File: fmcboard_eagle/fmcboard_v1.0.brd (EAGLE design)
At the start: 98 x 74 mm, 7 parts, among them J1 8pin, J12 4p-2.54, J2 ASP-134604-01

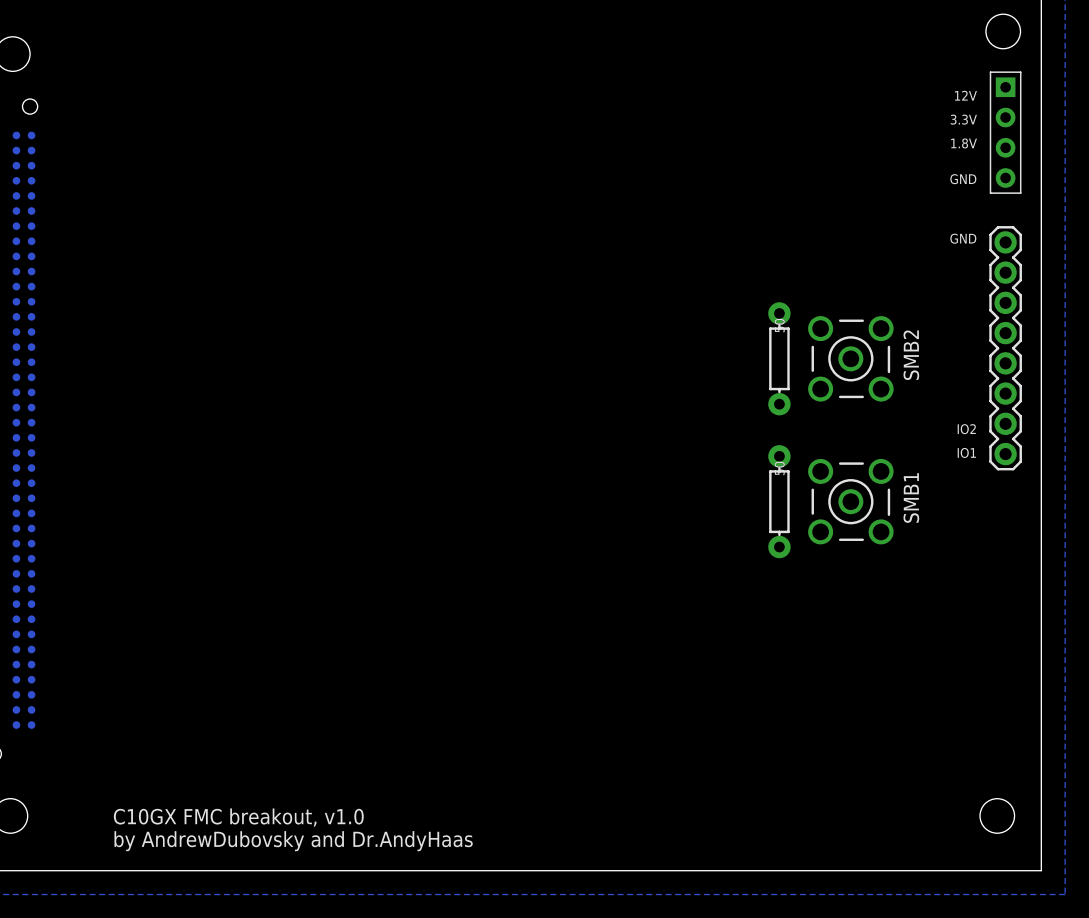
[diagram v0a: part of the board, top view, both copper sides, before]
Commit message: added two op amps to condition input and added GPIO breakout
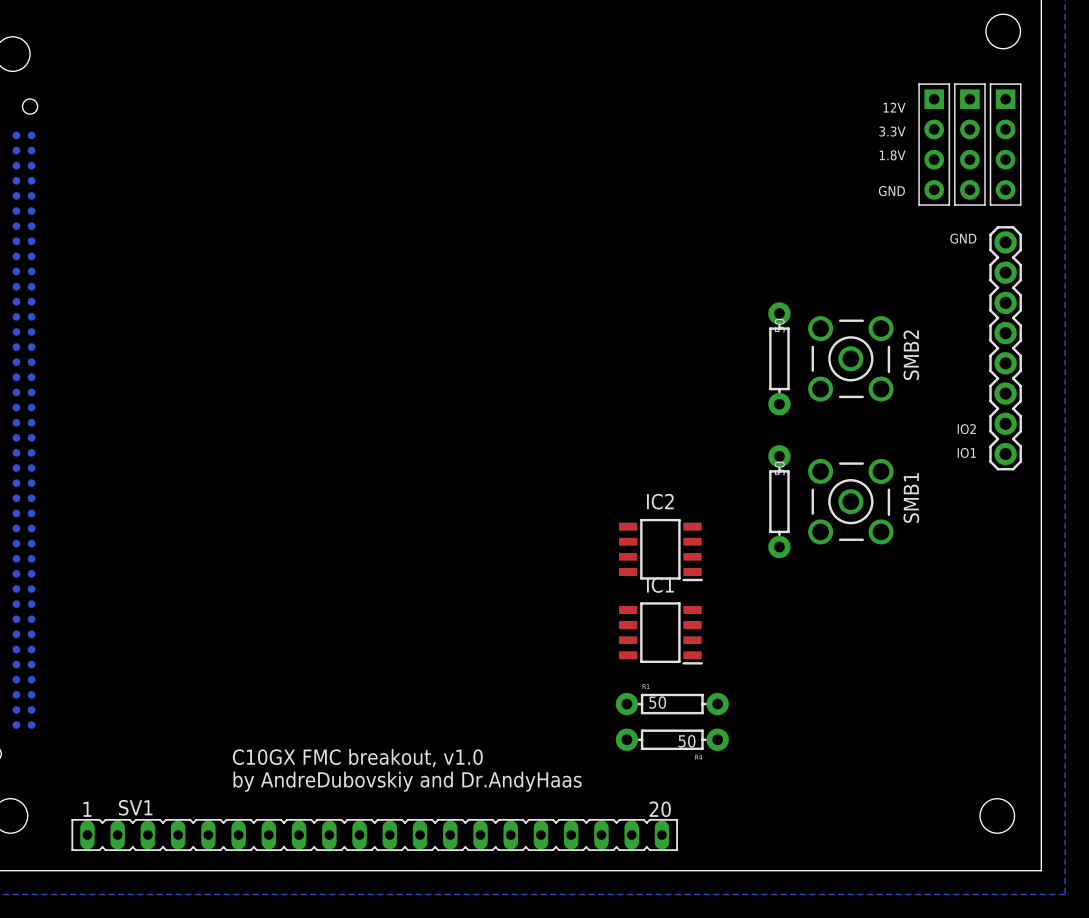
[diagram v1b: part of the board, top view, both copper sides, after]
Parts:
- added IC1, IC2: OPA699ID, OPA699ID:SOIC127P600X175-8N
- added J3, J4: 4p-2.54, Seeed-Connector:H4-2.54
- added R1, R4: 50, SparkFun-Resistors:AXIAL-0.3
- added SV1: (no value), con-lsta:FE20
- moved J12 6.08 mm to (89.0, 61.0)
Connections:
- removed net N$2: J1.3
- removed net N$4: J1.5
- removed net N$5: J1.4
- removed net N$6: J1.6
- new net +VS: IC1.7, IC2.7, J1.3
- new net -VS: IC1.4, IC2.4, J1.4
- new net N$1: IC1.3, IC2.2, IC2.6
- new net N$10: J2.H8, SV1.5
- new net N$11: J2.H4, SV1.3
- new net N$12: J2.H10, SV1.6
- new net N$13: J2.H11, SV1.7
- new net N$14: J2.H13, SV1.8
- new net N$15: J2.H14, SV1.9
- new net N$16: J2.H16, SV1.10
- new net N$17: J2.H17, SV1.11
- new net N$18: J2.H19, SV1.12
- new net N$19: J2.H20, SV1.13
- new net N$20: J2.H22, SV1.14
- new net N$21: J2.H23, SV1.15
- new net N$22: J2.H25, SV1.16
- new net N$23: J2.H26, SV1.17
- new net N$24: J2.H28, SV1.18
- new net N$25: J2.H29, SV1.19
- new net N$26: J2.H31, SV1.20
- new net N$3: IC1.2, R1.P$2, R4.P$1
- new net N$8: J2.H1, SV1.1
- new net N$9: J2.H2, SV1.2
- new net VH: IC1.8, IC2.8, J1.5
- new net VL: IC1.5, IC2.5, J1.6
- net 12V: now also J3.1, J4.1
- net 1V8: now also J3.3, J4.3
- net 3V3: now also J3.2, J4.2
- net GND: now also J2.H12, J2.H15, J2.H18, J2.H21, J2.H24, J2.H27, J2.H3, J2.H30, J2.H33, J2.H36, J2.H39, J2.H6, J2.H9, J3.4, J4.4, R4.P$2
- net IO1: now also IC2.3
- net IO2: now also IC1.6, J2.H7, R1.P$1, SV1.4
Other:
- board text added: "C10GX FMC breakout, v1.0 by AndreDubovskiy and Dr.AndyHaas"
- board text removed: "C10GX FMC breakout, v1.0 by AndrewDubovsky and Dr.AndyHaas"

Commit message: board v1 work with Andre
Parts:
- added C1, C2, C4, C6: 10uF, SparkFun-Capacitors:CAP-PTH-5MM
- added C10, C11, C12, C13, C14, C3, C5, C7, C8, C9: 0.1uF, SparkFun-Passives:0805
- added IC3, IC4: ICL7660CPA, maxim:DIL08
- added J5: 8pin, SparkFun-Connectors:1X08
- added PCB1: ARDUINO_NANO, E14_Arduino_revC:ARDUINO_NANO
- added R5: 10k, SparkFun-Resistors:AXIAL-0.3
- added R6: 50, SparkFun-Resistors:AXIAL-0.3
- added R7, R8: 100k, resistor:RTRIM3296W
- added SMB3: BU-SMB-V, con-coax:BU-SMB-V
- added SV2: 20, con-lsta:FE20
- added U1: TXS0108EPWR-TSSOP20, Seeed-IC:TSSOP20-0.65-6.5X4.4MM
- R1: value 50 -> 750
- R3: value 50 -> 10k
- R4: value 50 -> 150
- SV1: value (none) -> 20
- moved R3 112.7 mm to (2.00, -42.0), turned to 0 degrees
- moved J12 37.7 mm to (57.0, 41.0)
- moved J3 37.7 mm to (63.0, 41.0)
- moved J4 37.7 mm to (60.0, 41.0)
- moved SV1 30.6 mm to (23.0, 27.0), turned to 90 degrees
- moved R2 7.28 mm to (78.0, 38.0)
- moved SMB1 7.28 mm to (84.0, 38.0)
- moved SMB2 6.32 mm to (84.0, 49.0)
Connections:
- net N$16 renamed H16
- net N$17 renamed H17
- removed net IO2: IC1.6, J1.2, J2.H7, R1.P$1, R3.P$2, SMB2.1, SV1.4
- removed net N$10: J2.H8, SV1.5
- removed net N$11: J2.H4, SV1.3
- removed net N$12: J2.H10, SV1.6
- removed net N$13: J2.H11, SV1.7
- removed net N$14: J2.H13, SV1.8
- removed net N$15: J2.H14, SV1.9
- removed net N$18: J2.H19, SV1.12
- removed net N$19: J2.H20, SV1.13
- removed net N$20: J2.H22, SV1.14
- removed net N$21: J2.H23, SV1.15
- removed net N$22: J2.H25, SV1.16
- removed net N$23: J2.H26, SV1.17
- removed net N$24: J2.H28, SV1.18
- removed net N$25: J2.H29, SV1.19
- removed net N$26: J2.H31, SV1.20
- removed net N$7: J1.7
- removed net N$8: J2.H1, SV1.1
- removed net N$9: J2.H2, SV1.2
- new net AR_SCLIN: J5.7, PCB1.D9, U1.8
- new net AR_SDAIN: J5.6, PCB1.D11, U1.3
- new net H13: J2.H13, SV1.7
- new net H14: J2.H14, SV1.8
- new net H19: J2.H19, SV1.13
- new net H20: J2.H20, SV1.14
- new net H22: J2.H22, SV1.16
- new net H23: J2.H23, SV1.17
- new net H25: J2.H25, SV1.19
- new net H26: J2.H26, SV1.20
- new net H27: J2.H28, SV2.1
- new net H28: J2.H29, SV2.2
- new net H31: J2.H31, SV2.4
- new net H32: J2.H32, SV2.5
- new net H34: J2.H34, SV2.7
- new net H35: J2.H35, SV2.8
- new net H37: J2.H37, SV2.10
- new net H38: J2.H38, SV2.11
- new net IO2_H11: J2.H11, J5.2, R6.P$2, SMB3.1, SV1.5
- new net N$2: C4.1, IC3.2
- new net N$4: C4.2, IC3.4
- new net N$5: C1.1, IC4.2
- new net N$6: C1.2, IC4.4
- new net OFFSETIN1: C11.1, J5.4, R5.P$2
- new net OPBUF1: IC2.2, IC2.6, J5.5, R3.P$2
- new net OPOUT1_H10: IC1.6, J2.H10, J5.3, R1.P$1, SMB2.1, SV1.4
- new net SCLIN: J2.H7, SV1.1, U1.13
- new net SDAIN: J2.H8, SV1.2, U1.18
- net +VS: now also C3.1, C9.1, IC3.8, IC4.8, PCB1.5V, R7.3, U1.19
- net -VS: now also C10.1, C2.1, C6.1, IC3.5, IC4.5, R8.3
- net 12V: now also C12.1, J2.C37
- net 1V8: now also C14.1, C5.1, J2.H40, U1.10, U1.2
- net 3V3: now also C13.1, J2.D40
- net GND: now also C10.2, C11.2, C12.2, C13.2, C14.2, C2.2, C3.2, C5.2, C6.2, C7.2, C8.2, C9.2, IC3.3, IC4.3, J1.1, J1.2, J1.7, J5.8, PCB1.GND, R6.P$1, R7.1, R8.1, SMB3.2, SMB3.3, SMB3.4, SMB3.5, SV2.17, SV2.18, SV2.19, SV2.20, U1.11; no longer R3.P$1
- net IO1: now also J5.1; no longer J1.1
- net N$1: now also R3.P$1, R5.P$1; no longer IC2.2, IC2.6
- net VH: now also C7.1, R7.2
- net VL: now also C8.1, R8.2
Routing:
- added copper zone on layer 2, net GND

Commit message: first draft of pcb routing
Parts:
- removed PCB1: ARDUINO_NANO, E14_Arduino_revC:ARDUINO_NANO
- added ARDUINO_NANO1: (no value), ArduinoNanoV30:ARDUINO_NANO
- moved C14 152.6 mm to (58.0, 68.0), flipped to the bottom, turned to 180 degrees
- moved R8 141.5 mm to (55.0, 26.0), turned to 90 degrees
- moved C5 141.2 mm to (66.0, 66.0), flipped to the bottom, turned to 180 degrees
- moved R7 126.2 mm to (54.0, 14.0)
- moved C12 126.1 mm to (50.0, 45.0), turned to 180 degrees
- moved C13 125.9 mm to (50.0, 42.0), turned to 180 degrees
- moved C11 125.5 mm to (77.0, 15.0)
- moved C10 123.4 mm to (72.0, 21.0), turned to 270 degrees
- moved R6 106.8 mm to (38.0, 10.0), turned to 180 degrees
- moved C9 106.7 mm to (58.0, 18.0), turned to 180 degrees
- moved C8 106.2 mm to (57.0, 22.0), turned to 180 degrees
- moved SMB3 103.9 mm to (36.2, 15.8)
- moved C7 103.7 mm to (61.0, 17.0), turned to 270 degrees
- moved C3 100.4 mm to (60.0, 20.0), turned to 180 degrees
- moved R5 98.4 mm to (75.0, 21.0), turned to 270 degrees
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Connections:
- new net VIN: ARDUINO_NANO1.15
- net +VS: now also ARDUINO_NANO1.12; no longer PCB1.5V
- net AR_SCLIN: now also ARDUINO_NANO1.27; no longer PCB1.D9
- net AR_SDAIN: now also ARDUINO_NANO1.29; no longer PCB1.D11
- net GND: now also ARDUINO_NANO1.14, ARDUINO_NANO1.19; no longer PCB1.GND
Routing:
- net OPOUT1_H10: track 0.00 -> 198.7 mm, vias 0 -> 3
- net +VS: track 0.00 -> 185.5 mm, vias 0 -> 4
- net -VS: track 0.00 -> 146.0 mm, vias 0 -> 1
- net SCLIN: track 0.00 -> 132.4 mm, vias 0 -> 4
- net AR_SCLIN: track 0.00 -> 129.6 mm, vias 0 -> 5
- net SDAIN: track 0.00 -> 121.8 mm, vias 0 -> 2
- net IO2_H11: track 0.00 -> 120.1 mm, vias 0 -> 5
- net H38: track 0.00 -> 110.9 mm, vias 0 -> 1
- net VH: track 0.00 -> 108.3 mm, vias 0 -> 4
- net 1V8: track 0.00 -> 102.3 mm, vias 0 -> 4
- net AR_SDAIN: track 0.00 -> 88.1 mm, vias 0 -> 5
- net 12V: track 0.00 -> 68.0 mm, vias 0 -> 1
- net 3V3: track 0.00 -> 66.2 mm, vias 0 -> 1
- net VL: track 0.00 -> 64.0 mm, vias 0 -> 5
- net GND: track 0.00 -> 56.5 mm
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- removed copper zone on layer 2, net GND
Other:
- board text added: "C10GX FMC breakout, v1.0 by Andre Dubovskiy and Dr. Andy Haas"
- board text removed: "C10GX FMC breakout, v1.0 by AndreDubovskiy and Dr.AndyHaas"

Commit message: fmcboard v1 submitted
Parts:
- removed SMB1, SMB2, SMB3: BU-SMB-V, con-coax:BU-SMB-V
- added IO_H11, OPIN, OPOUT_H10: BU-SMB-V, con-coax:BU-SMB-V
- U1: value TXS0108EPWR-TSSOP20 -> TXS0108EPWR
- moved C9 45.0 mm to (56.0, 63.0), flipped to the bottom, turned to 0 degrees
- moved C7 29.7 mm to (45.0, 42.0), turned to 180 degrees
- moved C5 29.0 mm to (45.0, 46.0), flipped to the top
- moved C8 25.1 mm to (45.0, 44.0)
- moved C3 15.6 mm to (70.0, 32.0), turned to 0 degrees
- moved C11 14.8 mm to (70.0, 28.0)
- moved R5 12.4 mm to (63.0, 18.0), turned to 0 degrees
- moved R7 12.0 mm to (45.0, 22.0), turned to 90 degrees
- moved R8 10.8 mm to (45.0, 30.0)
- moved R2 10.0 mm to (70.0, 46.0)
- moved C10 9.22 mm to (70.0, 30.0), turned to 0 degrees
- moved R6 8.25 mm to (30.0, 8.00), turned to 90 degrees
- moved IC1 8.06 mm to (62.0, 27.0)
- moved C13 7.81 mm to (45.0, 48.0)
- moved C12 7.07 mm to (45.0, 50.0)
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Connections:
- net GND: now also IO_H11.2, IO_H11.3, IO_H11.4, IO_H11.5, OPIN.2, OPIN.3, OPIN.4, OPIN.5, OPOUT_H10.2, OPOUT_H10.3, OPOUT_H10.4, OPOUT_H10.5; no longer SMB1.2, SMB1.3, SMB1.4, SMB1.5, SMB2.2, SMB2.3, SMB2.4, SMB2.5, SMB3.2, SMB3.3, SMB3.4, SMB3.5
- net IO1: now also OPIN.1; no longer SMB1.1
- net IO2_H11: now also IO_H11.1; no longer SMB3.1
- net OPOUT1_H10: now also OPOUT_H10.1; no longer SMB2.1
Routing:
- net H38: track 110.9 -> 20.9 mm
- net OPOUT1_H10: track 198.7 -> 131.9 mm, vias 3 -> 1
- net AR_SCLIN: track 129.6 -> 84.4 mm, vias 5 -> 1
- net GND: track 56.5 -> 100.3 mm, vias 0 -> 4
- net OPBUF1: track 51.9 -> 94.9 mm, vias 4 -> 1
- net VL: track 64.0 -> 100.0 mm, vias 5 -> 0
- net SDAIN: track 121.8 -> 97.0 mm
- net SCLIN: track 132.4 -> 108.6 mm, vias 4 -> 2
- net -VS: track 146.0 -> 123.0 mm, vias 1 -> 0
- net OFFSETIN1: track 24.9 -> 47.1 mm
- net IO2_H11: track 120.1 -> 99.5 mm, vias 5 -> 1
- net H31: track 51.3 -> 32.1 mm
- net H35: track 39.4 -> 24.8 mm
- net VH: track 108.3 -> 94.4 mm, vias 4 -> 3
- net 12V: track 68.0 -> 81.9 mm
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- added copper zone on layer 2, net GND
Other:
- board outline removed
- board text added: "+VS 5"
- board text added: "-VS -5"
- board text added: "AR SCLIN"
- board text added: "AR SDAIN"
- board text added: "C10GX FMC breakout, v1.0 by Andre Dubovskiy and Dr. Andy Haas NYU, 2023"
- board text added: "H10"
- board text added: "H11"
- board text added: "H13"
- board text added: "H14"
- board text added: "H16"
- board text added: "H17"
- board text added: "H19"
- board text added: "H20"
- board text added: "H22"
- board text added: "H23"
- board text added: "H25"
- board text added: "H26"
- board text added: "H27"
- board text added: "H28"
- board text added: "H31"
- board text added: "H32"
- board text added: "H34"
- board text added: "H35"
- board text added: "H37"
- board text added: "H38"
- board text added: "H7"
- board text added: "H8"
- board text added: "IO H11"
- board text added: "OFFSETIN1"
- board text added: "OPBUF1"
- board text added: "OPIN"
- board text added: "OPOUT H10"
- board text added: "VH"
- board text added: "VL"
- board text removed: "C10GX FMC breakout, v1.0 by Andre Dubovskiy and Dr. Andy Haas"
- board text removed: "IO1"
- board text removed: "IO2"

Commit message: fmcboard v1 submitted again, with board outline and stencil
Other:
- board outline added: 98 x 74 mm
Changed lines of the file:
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@@
 <board>
 <plain>
-<wire x1="0" y1="74" x2="0" y2="0" width="0" layer="21"/>
-<wire x1="0" y1="0" x2="98" y2="0" width="0" layer="21"/>
-<wire x1="98" y1="0" x2="98" y2="74" width="0" layer="21"/>
-<wire x1="98" y1="74" x2="0" y2="74" width="0" layer="21"/>
+<wire x1="0" y1="74" x2="0" y2="0" width="0.3048" layer="20"/>
+<wire x1="0" y1="0" x2="98" y2="0" width="0.3048" layer="20"/>
+<wire x1="98" y1="0" x2="98" y2="74" width="0.3048" layer="20"/>
+<wire x1="98" y1="74" x2="0" y2="74" width="0.3048" layer="20"/>
 <hole x="11.4" y="4.6" drill="2.9"/>
 <hole x="94.8" y="70.5" drill="2.9"/>
